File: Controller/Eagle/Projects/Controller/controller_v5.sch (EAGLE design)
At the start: 71 parts, among them J2 AVR_SPI_PRG_6NS, J3 GIMBAL_3PIN, J4 GIMBAL_3PIN, J5 GIMBAL_3PIN, J6 GIMBAL_3PIN, U2 ATMEGA128RFA1, U3 RF_AMPLIFIER, Y1 32.768kHz, Y2 16MHz

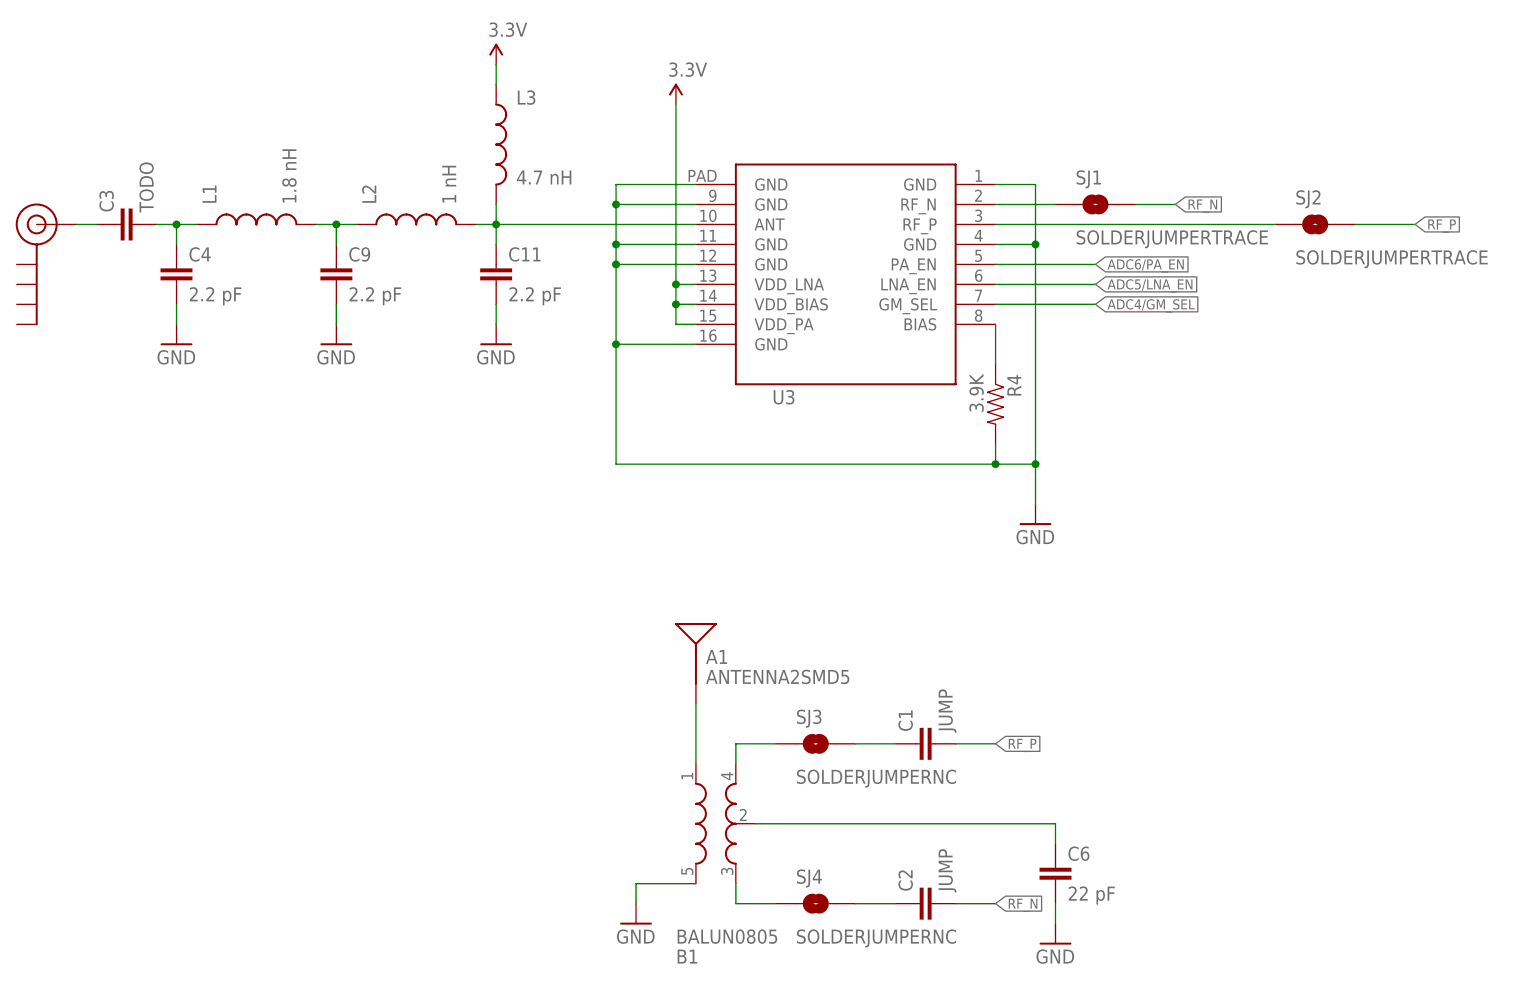
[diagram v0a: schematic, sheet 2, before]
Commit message: Adding v5 of the controller board, which only has one antenna
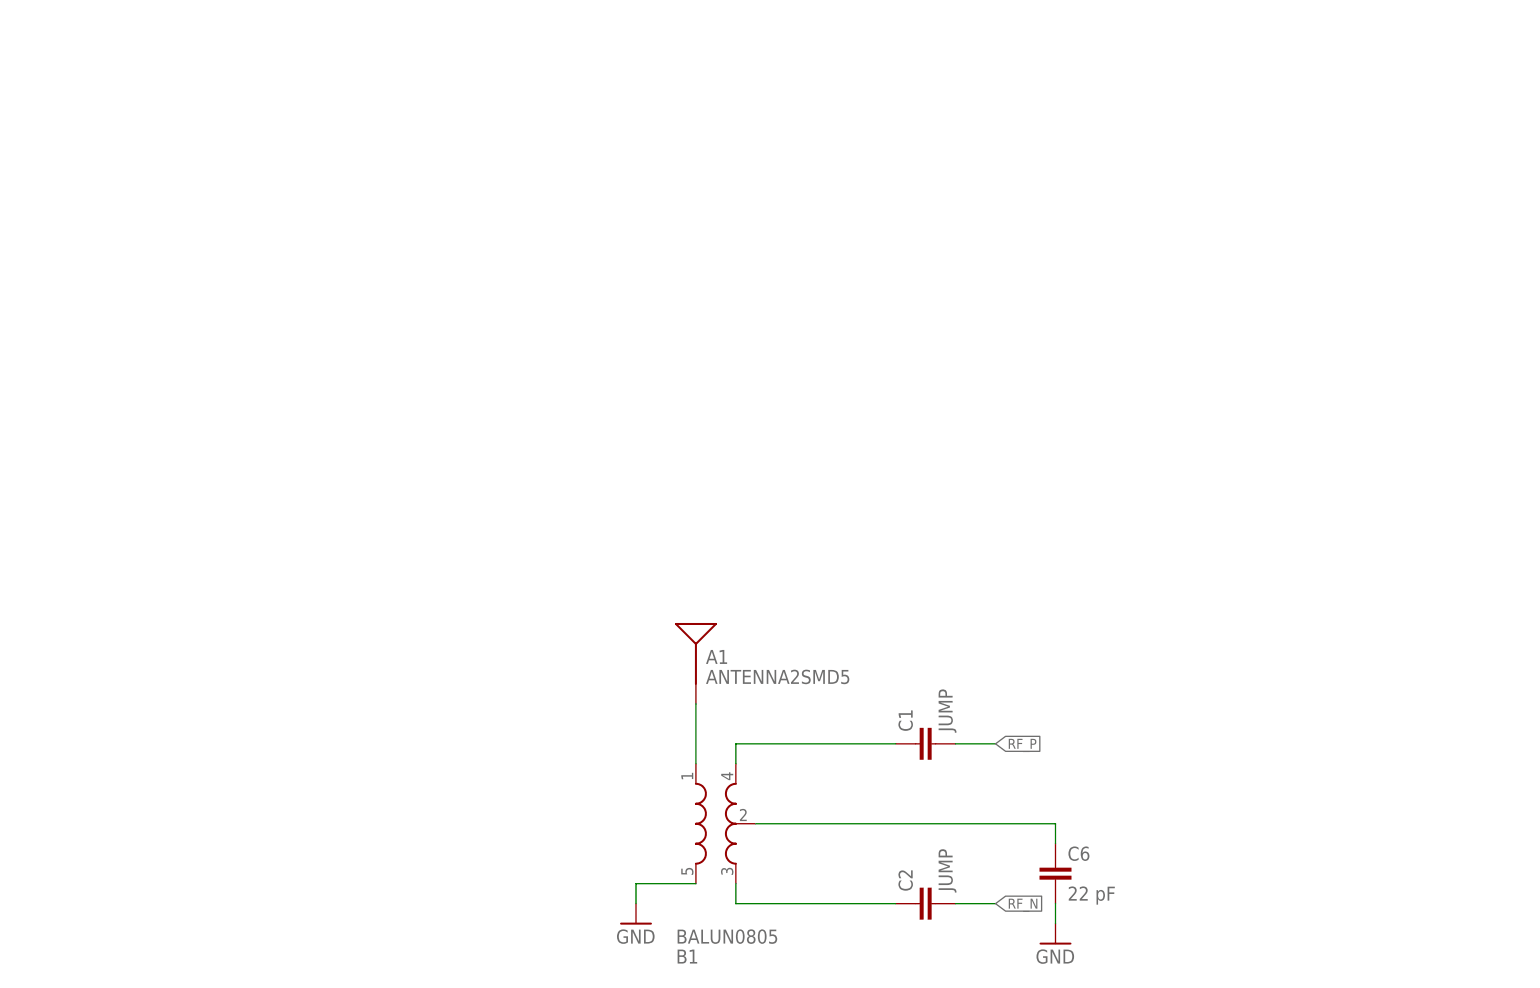
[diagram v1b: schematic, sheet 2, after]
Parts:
- removed C11, C4, C9: 2.2 pF, Controller:CAP0805
- removed C3: TODO, Controller:CAP0805
- removed J$1: SMA_EDGE, Controller:SMA_EDGE
- removed L1: 1.8 nH, Controller:INDUCTOR0805
- removed L2: 1 nH, Controller:INDUCTOR0805
- removed L3: 4.7 nH, Controller:INDUCTOR0805
- removed R16: 10K, SparkFun:TRIMPOT-PTH-KNOB
- removed R4: 3.9K, Controller:RESISTOR0805-RES
- removed SJ1, SJ2: SOLDERJUMPERTRACE, Controller:SOLDERJUMPERTRACE
- removed SJ3, SJ4: SOLDERJUMPERNC, Controller:SOLDERJUMPERNC
- removed U3: RF_AMPLIFIER, Controller:CC2592QF
- added R1: 10K, Controller:TRIMPOT-PTH-KNOB
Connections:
- removed net N$1: C9.1, L1.2, L2.1
- removed net N$13: C1.1, SJ3.2
- removed net N$14: C2.1, SJ4.2
- removed net N$17: SJ2.1, U3.RF_P@3
- removed net N$3: C11.1, L2.2, L3.2, U3.ANT@10
- removed net N$4: C3.2, C4.1, L1.1
- removed net N$6: SJ1.1, U3.RF_N@2
- removed net N$7: R4.1, U3.BIAS@8
- removed net N$8: C3.1, J$1.SIGNAL
- removed net TST: U2.TST
- net 3.3V: no longer L3.1, U3.VDD_BIAS@14, U3.VDD_LNA@13, U3.VDD_PA@15
- net ADC4/GM_SEL: no longer U3.GM_SEL@7
- net ADC5/LNA_EN: no longer U3.LNA_EN@6
- net ADC6/PA_EN: no longer U3.PA_EN@5
- net GND: now also R1.CW, U2.TST; no longer C11.2, C4.2, C9.2, R16.CW, R4.2, U3.GND@1, U3.GND@11, U3.GND@12, U3.GND@16, U3.GND@4, U3.GND@9, U3.GND@PAD
- net N$10: now also C2.1; no longer SJ4.1
- net N$9: now also C1.1; no longer SJ3.1
- net RF_N: no longer SJ1.2
- net RF_P: no longer SJ2.2
- net VCC: now also R1.CCW; no longer R16.CCW
- net VCUTOFF: now also R1.WIPER; no longer R16.WIPER

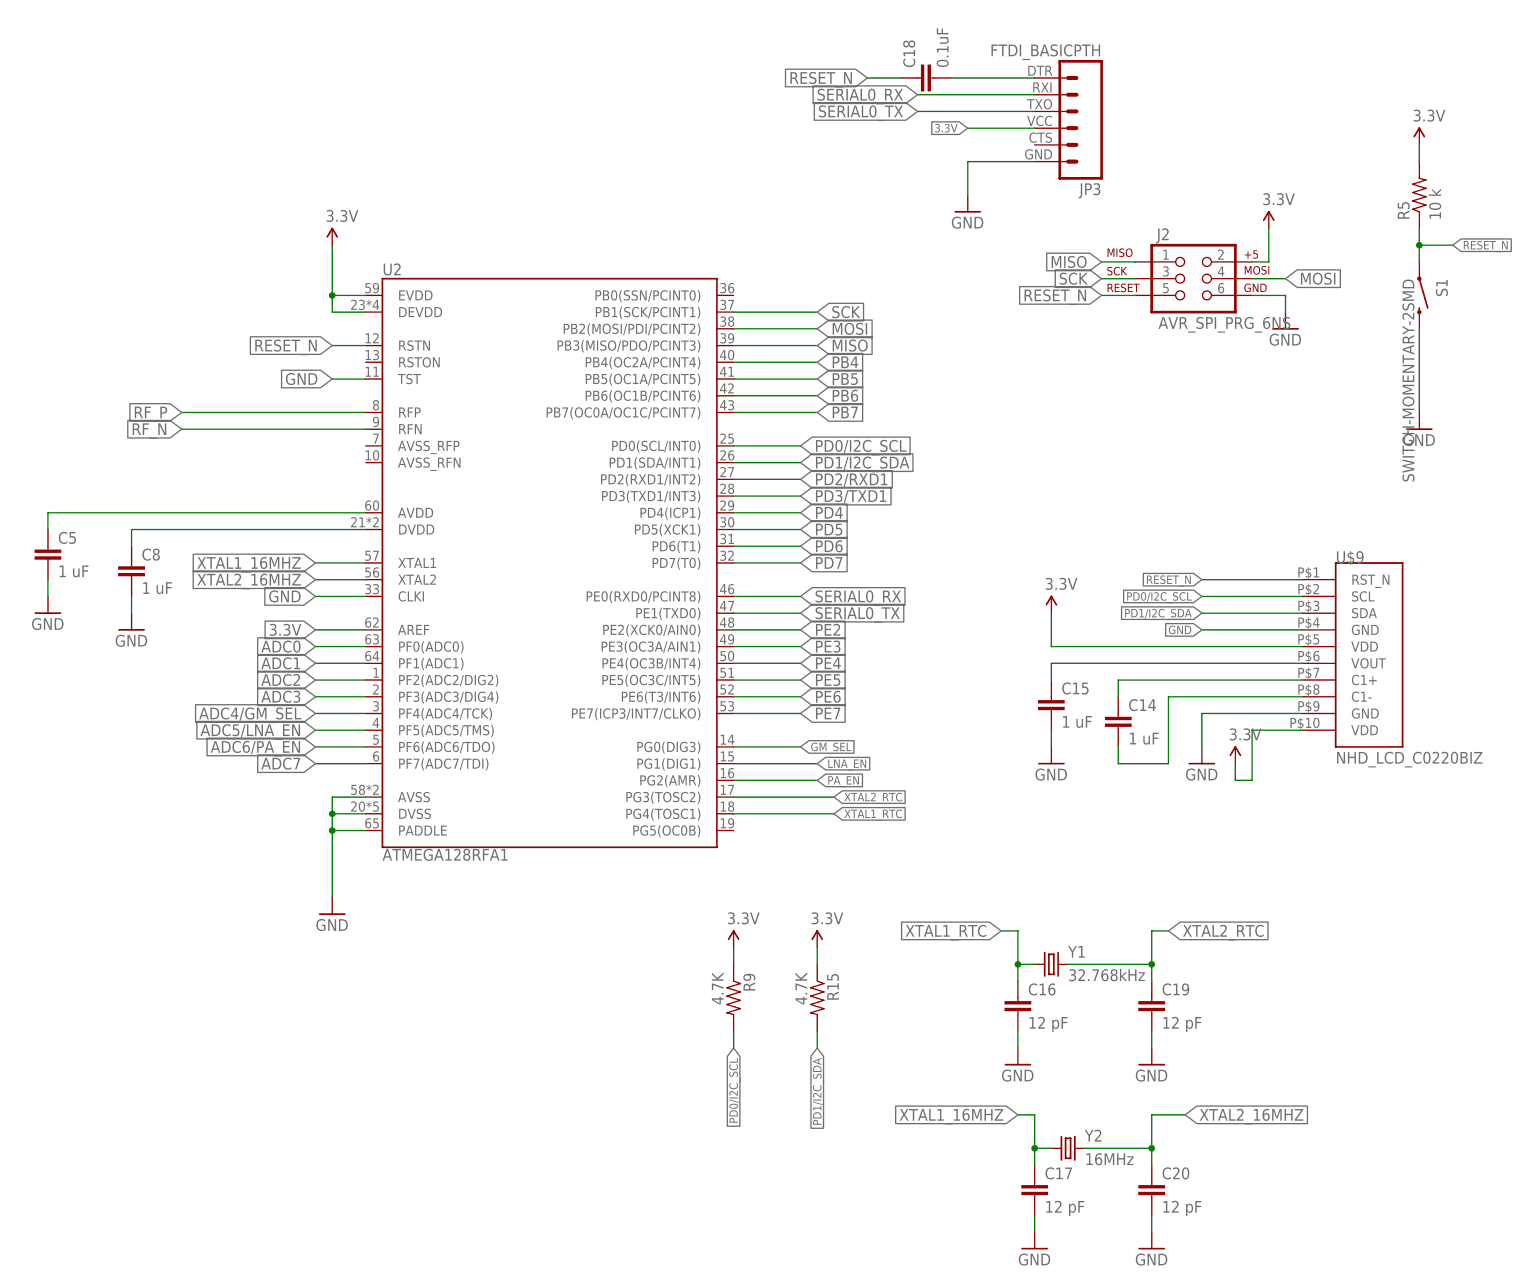
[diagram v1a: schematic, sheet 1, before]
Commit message: In the controller, finished connecting unconnected pins and Passed DRC using the Seeedstudio DRC files.
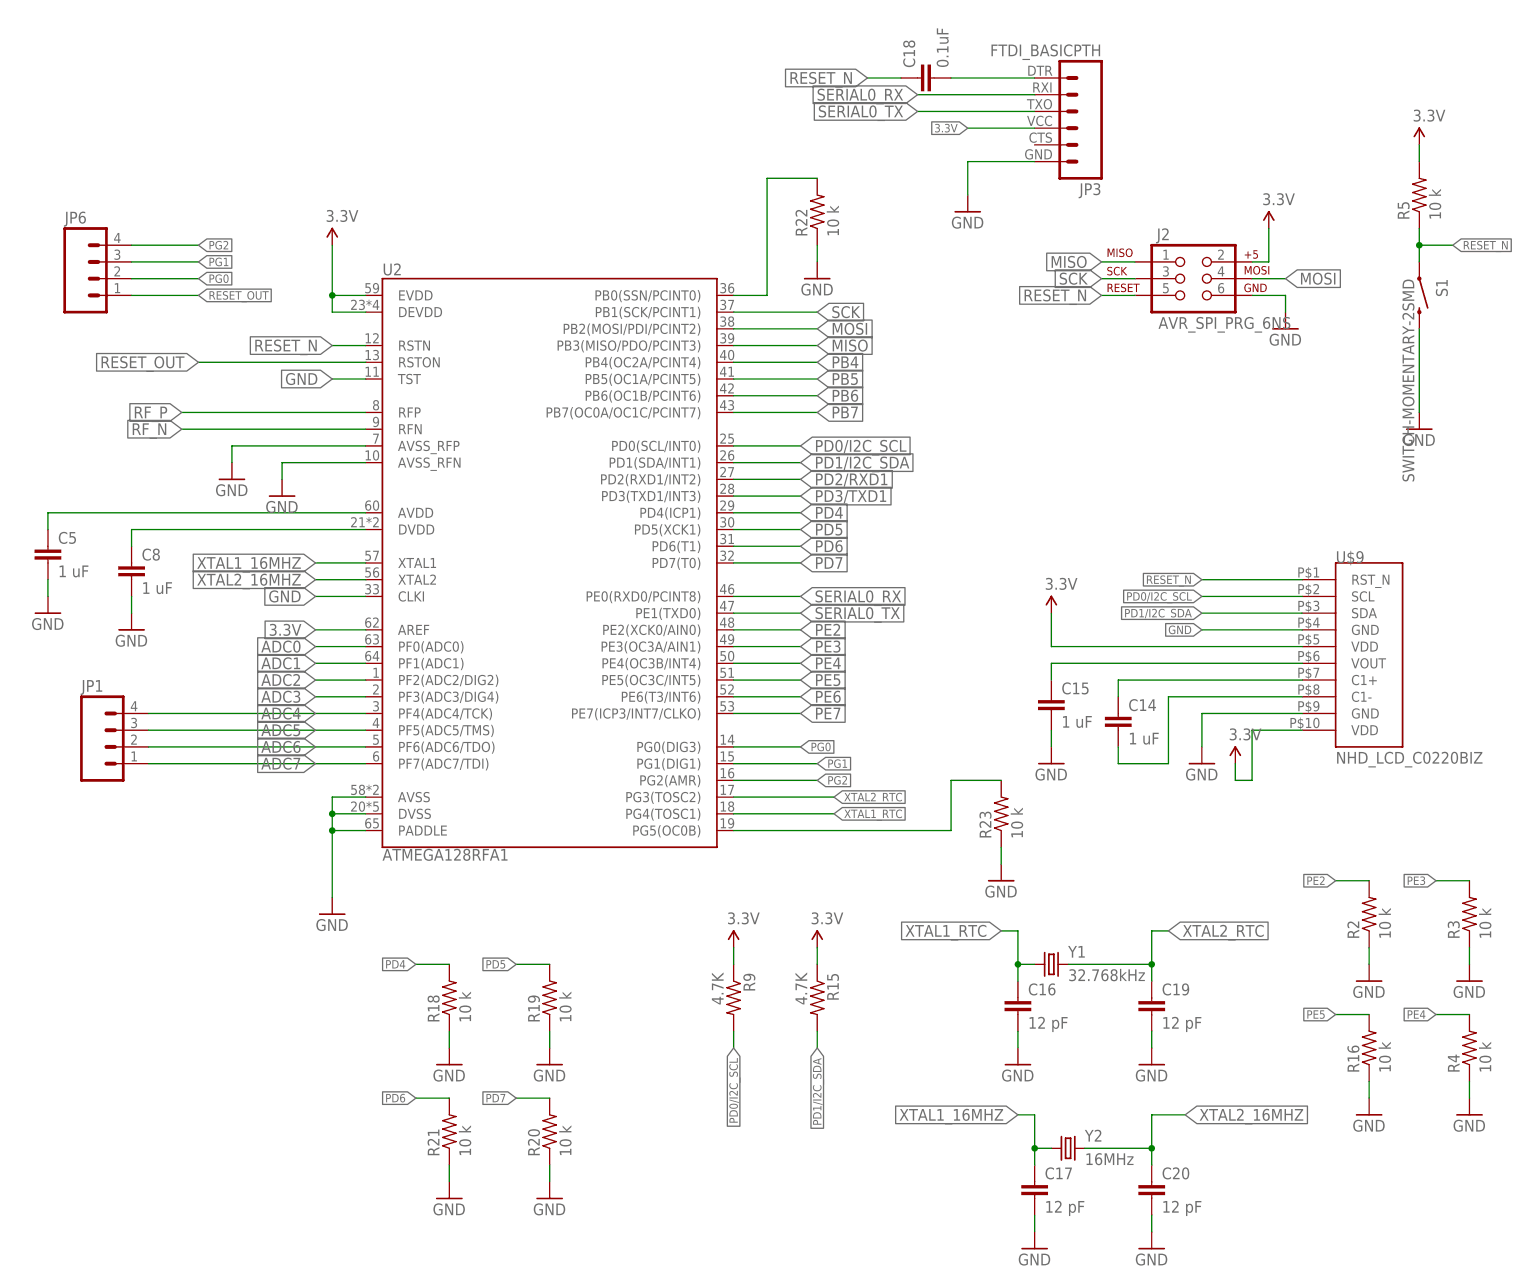
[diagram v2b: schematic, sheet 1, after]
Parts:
- added JP1, JP6: (no value), Controller:M04PTH
- added R16, R18, R19, R2, R20, R21, R22, R23, R3, R4: 10 k, Controller:RESISTOR0805-RES
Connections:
- removed net ADC4/GM_SEL: U2.PF4(ADC4/TCK)
- removed net ADC5/LNA_EN: U2.PF5(ADC5/TMS)
- removed net ADC6/PA_EN: U2.PF6(ADC6/TDO)
- removed net GM_SEL: U2.PG0(DIG3)
- removed net LNA_EN: U2.PG1(DIG1)
- removed net PA_EN: U2.PG2(AMR)
- new net ADC4: JP1.4, U2.PF4(ADC4/TCK)
- new net ADC5: JP1.3, U2.PF5(ADC5/TMS)
- new net ADC6: JP1.2, U2.PF6(ADC6/TDO)
- new net PB0: R22.2, U2.PB0(SSN/PCINT0)
- new net PB1: R23.2, U2.PG5(OC0B)
- new net PG0: JP6.2, U2.PG0(DIG3)
- new net PG1: JP6.3, U2.PG1(DIG1)
- new net PG2: JP6.4, U2.PG2(AMR)
- new net RESET_OUT: JP6.1, U2.RSTON
- net ADC7: now also JP1.1
- net GND: now also R16.1, R18.1, R19.1, R2.1, R20.1, R21.1, R22.1, R23.1, R3.1, R4.1, U2.AVSS_RFN, U2.AVSS_RFP
- net PD4: now also R18.2
- net PD5: now also R19.2
- net PD6: now also R21.2
- net PD7: now also R20.2
- net PE2: now also R2.2
- net PE3: now also R3.2
- net PE4: now also R4.2
- net PE5: now also R16.2

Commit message: Added additional resistors to the gimbals to create a resistor ladder and meet the ADC swing voltage requirements.
Also, cleaned up some of the board routing.
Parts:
- added JP7: M01PTH, Controller:M01PTH
- added R24, R25, R26, R27: 5K, Controller:RESISTOR0805-RES
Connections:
- new net AREF: JP7.1, U2.AREF
- new net N$1: J6.VDD, R24.1
- new net N$3: J3.VDD, R25.1
- new net N$4: J5.VDD, R26.1
- new net N$6: J4.VDD, R27.1
- net 3.3V: now also R24.2, R25.2, R26.2, R27.2; no longer J3.VDD, J4.VDD, J5.VDD, J6.VDD, U2.AREF
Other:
- moved on the sheet: U$1, U$3
